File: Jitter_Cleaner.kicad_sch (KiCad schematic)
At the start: 38 parts, among them T1 TCM2-43X+, T3 TCM2-43X+, U18 SI5394, U20 TLV75733PDBV, U21 TLV75718PDBV, Y1 CX3225SB48000D0FPJC1

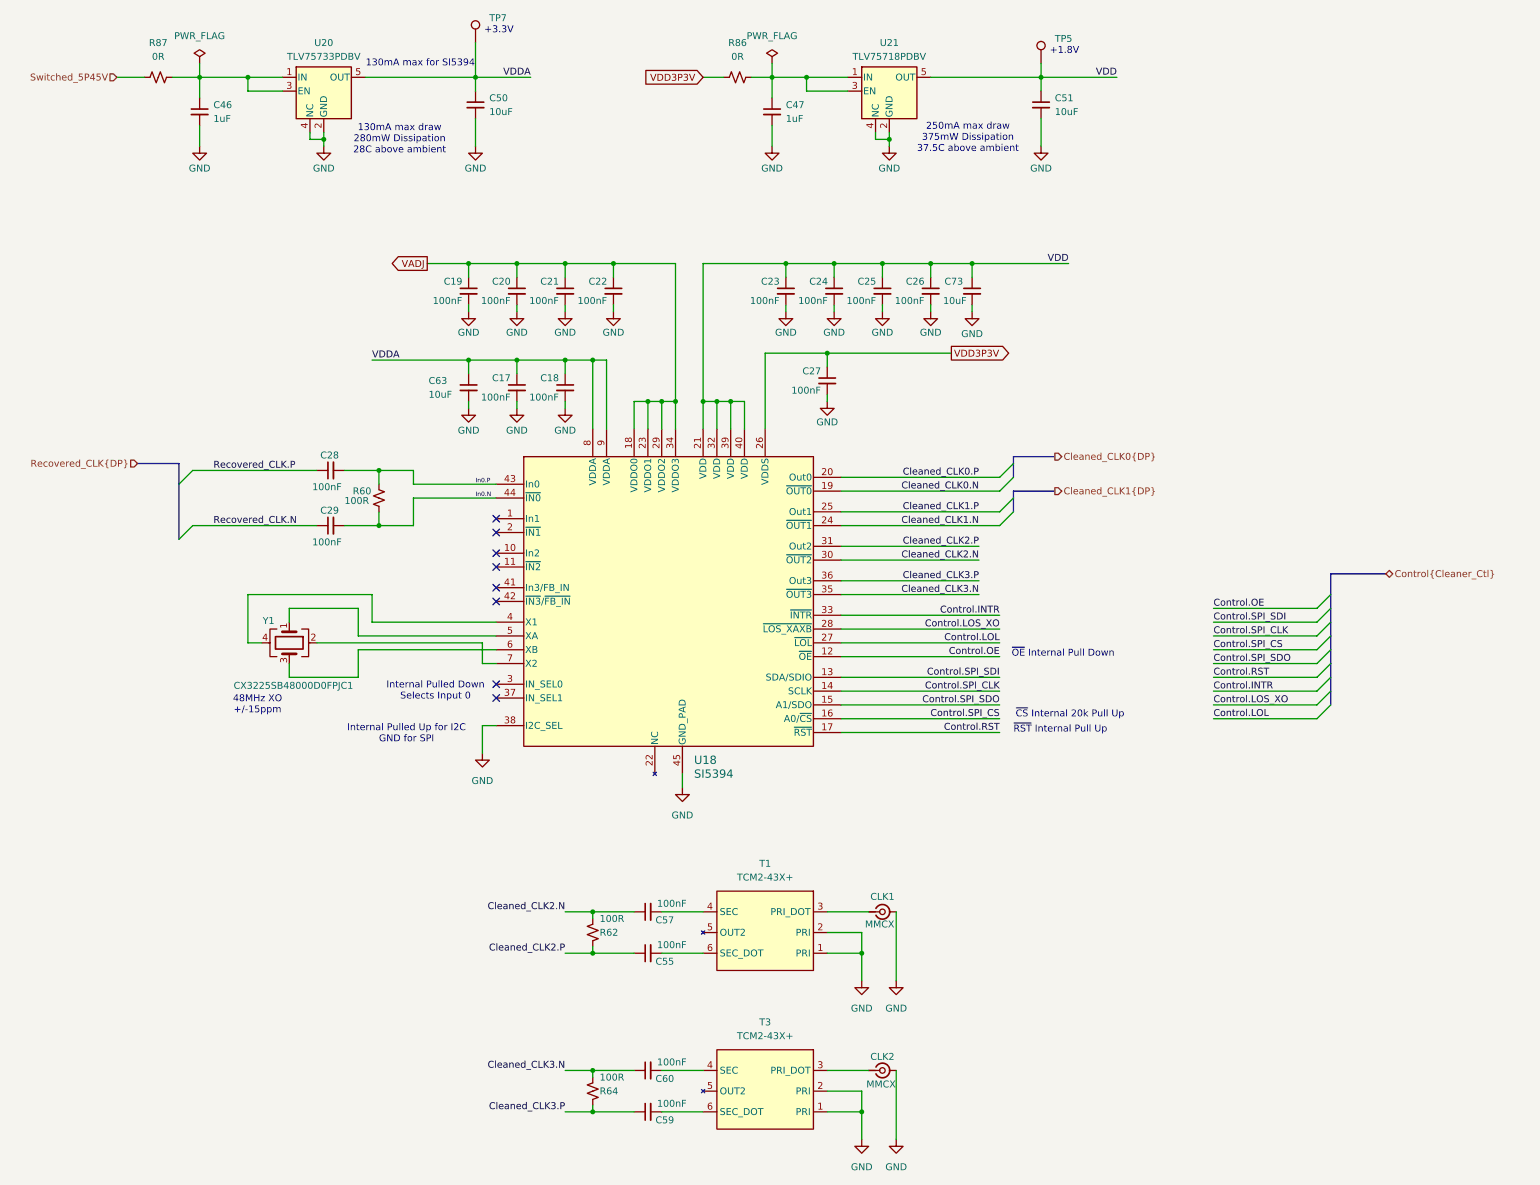
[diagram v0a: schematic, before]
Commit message: Updates after external review
- Changed Value of R66 & R67
- Added 100nF cap (C104) at input of U22
- Added GND via in center of U24 (like other LDO's)
- Changed 1nF Caps in Digital output section to 10nF
- Rounded pads of (T1-T4)
- Adjusted traces between T1-T4 and their respective MMCX connector
- Added FB1 & C136 at output of U22(5.45V switcher)
- Exchanged R88(0ohm) for a Ferrite Bead at input to U22(5.45V switcher)
- Revised layout of U22 area to more closely follow the data sheet.
- Exchanged R73&R42 at input to U44 for a ferrite bead (FB3)
- Exchanged R86/87/98/99 at input of TLV757 LDO for ferrite beads
- Added 1uF caps to VDD, VDDA, and VDDS power rails on Jitter Cleaner
- Changed C46,C47,C75,C77 from 1uF to 10uF caps
- Added Ferrite and 2 caps for each VDDO power rail on the jitter cleaners
- Adjusted layout around pint 26,27,28, of U18
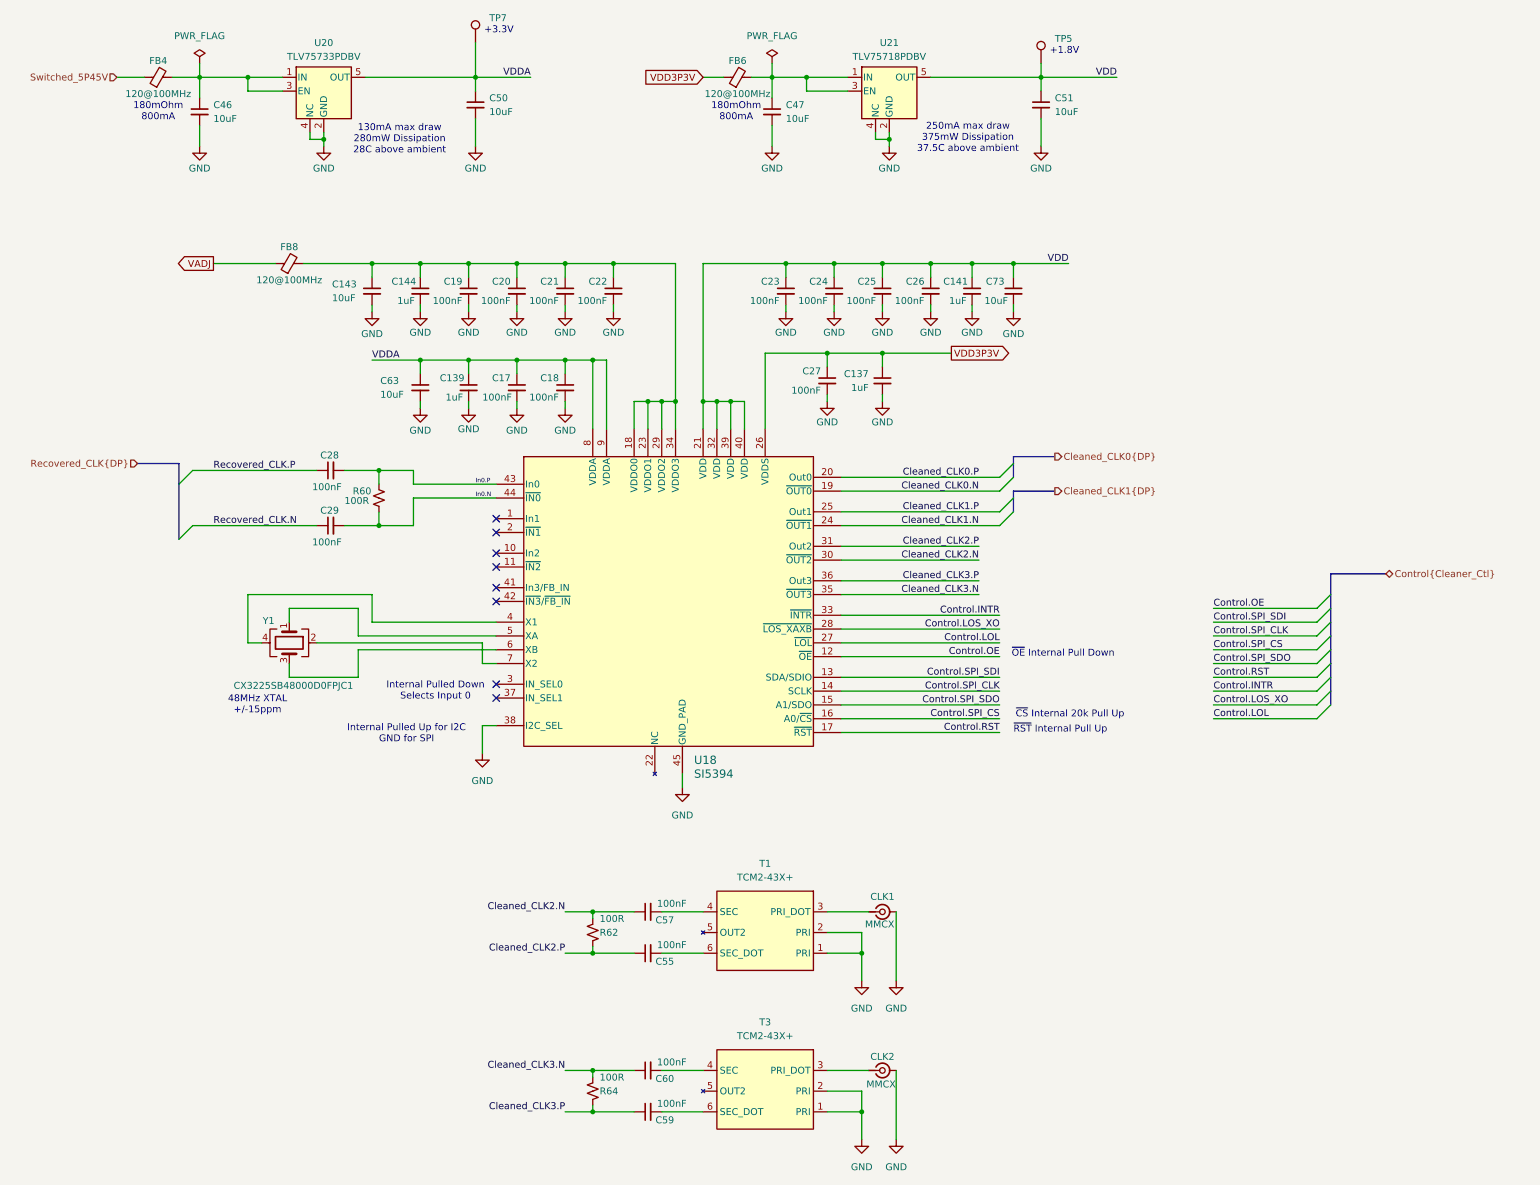
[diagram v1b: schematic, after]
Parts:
- removed R86, R87: 0R, Resistor_SMD:R_0603_1608Metric, symbol Device:R_Small_US
- added C137, C139, C141, C144: 1uF, Capacitor_SMD:C_0603_1608Metric, symbol Device:C_Small
- added C143: 10uF, Capacitor_SMD:C_0805_2012Metric, symbol Device:C_Small
- added FB4, FB6, FB8: 120@100MHz, Inductor_SMD:L_0603_1608Metric, symbol Device:FerriteBead_Small
- C46, C47: value 1uF -> 10uF; footprint Capacitor_SMD:C_0603_1608Metric -> Capacitor_SMD:C_0805_2012Metric; MPN GCM188R71C105KA64D -> GRM21BR61E106KA73L
- T1, T3: footprint RF_Mini-Circuits:Mini-Circuits_DB1627 -> rf-input-fmc:Mini-Circuits_DB1627_rounded_pads
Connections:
- net GND: now also C137.2, C139.2, C141.2, C143.2, C144.2
- net Switched_5P45V: now also FB4.1
- net VADJ: now also FB8.1; no longer C19.1, C20.1, C21.1, C22.1, U18.18 (VDDO0), U18.23 (VDDO1), U18.29 (VDDO2), U18.34 (VDDO3)
- net VDD: now also C141.1
- net VDD3P3V: now also C137.1, FB6.1
- net VDDA: now also C139.1
- net at C47.1, U21.1 (IN), U21.3 (EN): now also FB6.2
- net at C46.1, U20.1 (IN), U20.3 (EN): now also FB4.2
- new net: C143.1, C144.1, C19.1, C20.1, C21.1, C22.1, FB8.2, U18.18 (VDDO0), U18.23 (VDDO1), U18.29 (VDDO2), U18.34 (VDDO3)
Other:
- note added: "180mOhm 800mA"
- note added: "48MHz XTAL +/-15ppm"
- note removed: "130mA max for SI5394"
- note removed: "48MHz XO +/-15ppm"
- moved on the sheet: C63, C73

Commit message: Updates after external review
- Removed various construction lines on comments layer
- Corrected various 50ohm SE traces on external layers to 0.26mm width
- Shortened up longer traces where possible on external layers and LVDS (in5)
- Made routing of CLK signals to MMCX test ports consistant

- MAJOR UPDATE to XTAL (Y1&Y2)
This now follows the family reference manual to properly isolate the XTAL
This then required the following changes:
- Swapped layer In2 with In5 (to keep LVDS between GND layers)
- Swapped layer In3 with In4 (to keep LVDS between GND layers)
- Revised gate mapping of level shifted signals on the IC (no FMC pinout change)
- Significant revision to  routing around these area
- Rounded XTAL pads
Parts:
- Y1: footprint Crystal:Crystal_SMD_Abracon_ABM8AIG-4Pin_3.2x2.5mm -> rf-input-fmc:Crystal_SMD_Abracon_ABM8AIG-4Pin_3.2x2.5mm
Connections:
- net at U18.4 (X1), Y1.4: now also U18.7 (X2), Y1.2
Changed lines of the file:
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@@
 	(text "48MHz XTAL\n+/-15ppm"
 		(exclude_from_sim no)
-		(at 154.178 165.1 0)
+		(at 140.208 156.972 0)
 		(effects
 			(font
@@
 	)
 	(junction
+		(at 152.4 153.67)
+		(diameter 0)
+		(color 0 0 0 0)
+	)
+	(junction
 		(at 201.93 101.6)
 		(diameter 0)
@@
 	)
 	(junction
+		(at 167.64 144.78)
+		(diameter 0)
+		(color 0 0 0 0)
+	)
+	(junction
 		(at 236.22 109.22)
 		(diameter 0)
@@
 	(wire
 		(pts
-			(xy 165.1 153.67) (xy 195.58 153.67)
-		)
-		(stroke
-			(width 0)
-			(type default)
-		)
-	)
-	(wire
-		(pts
 			(xy 330.2 157.48) (xy 349.25 157.48)
 		)
@@
 	(wire
 		(pts
+			(xy 152.4 161.29) (xy 152.4 153.67)
+		)
+		(stroke
+			(width 0)
+			(type default)
+		)
+	)
+	(wire
+		(pts
 			(xy 238.76 109.22) (xy 236.22 109.22)
 		)
@@
 	(wire
 		(pts
+			(xy 173.99 157.48) (xy 173.99 161.29)
+		)
+		(stroke
+			(width 0)
+			(type default)
+		)
+	)
+	(wire
+		(pts
 			(xy 143.51 46.99) (xy 143.51 49.53)
 		)
@@
 	(wire
 		(pts
-			(xy 152.4 144.78) (xy 175.26 144.78)
+			(xy 152.4 144.78) (xy 167.64 144.78)
 		)
 		(stroke
@@
 	(wire
 		(pts
-			(xy 349.25 160.02) (xy 330.2 160.02)
+			(xy 173.99 161.29) (xy 152.4 161.29)
 		)
 		(stroke
@@
 		)
 	)
-	(bus
+	(wire
 		(pts
-			(xy 361.95 140.97) (xy 351.79 140.97)
+			(xy 349.25 160.02) (xy 330.2 160.02)
 		)
 		(stroke
@@
 		)
 	)
-	(wire
+	(bus
 		(pts
-			(xy 195.58 153.67) (xy 195.58 157.48)
+			(xy 361.95 140.97) (xy 351.79 140.97)
 		)
 		(stroke
@@
 	(wire
 		(pts
+			(xy 167.64 144.78) (xy 175.26 144.78)
+		)
+		(stroke
+			(width 0)
+			(type default)
+		)
+	)
+	(wire
+		(pts
 			(xy 255.27 49.53) (xy 262.89 49.53)
 		)
@@
 	(wire
 		(pts
+			(xy 167.64 153.67) (xy 167.64 144.78)
+		)
+		(stroke
+			(width 0)
+			(type default)
+		)
+	)
+	(wire
+		(pts
 			(xy 269.24 83.82) (xy 260.35 83.82)
 		)
@@
 	(wire
 		(pts
-			(xy 195.58 157.48) (xy 198.12 157.48)
+			(xy 173.99 157.48) (xy 198.12 157.48)
 		)
 		(stroke
@@
 	(wire
 		(pts
+			(xy 165.1 153.67) (xy 167.64 153.67)
+		)
+		(stroke
+			(width 0)
+			(type default)
+		)
+	)
+	(wire
+		(pts
 			(xy 259.08 100.33) (xy 259.08 102.87)
 		)
@@
 		)
 		(property "Value" "CX3225SB48000D0FPJC1"
-			(at 160.782 161.544 90)
+			(at 139.7 153.67 90)
 			(effects
 				(font
@@
 			)
 		)
-		(property "Footprint" "Crystal:Crystal_SMD_Abracon_ABM8AIG-4Pin_3.2x2.5mm"
+		(property "Footprint" "rf-input-fmc:Crystal_SMD_Abracon_ABM8AIG-4Pin_3.2x2.5mm"
 			(at 160.02 153.67 0)
 			(effects

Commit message: Small Tweaks
- Updated readme with kicad version
- fixed break in ground plane near Y2
- added exclusions with written exceptions for 4 DRC errors (where we grounded level shifter gates)
- Fixed whitespace at the end of MPNs
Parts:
- FB4, FB6, FB8: MPN BLM18AG121SN1D -> BLM18AG121SN1D
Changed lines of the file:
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@@
 			)
 		)
-		(property "MPN" "BLM18AG121SN1D "
+		(property "MPN" "BLM18AG121SN1D"
 			(at 135.89 49.53 90)
 			(effects
@@
 			)
 		)
-		(property "MPN" "BLM18AG121SN1D "
+		(property "MPN" "BLM18AG121SN1D"
 			(at 242.57 49.53 90)
 			(effects
@@
 			)
 		)
-		(property "MPN" "BLM18AG121SN1D "
+		(property "MPN" "BLM18AG121SN1D"
 			(at 160.02 83.82 90)
 			(effects

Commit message: Changed LDO gnd pours
-LDO ground pours had odd gerber outputs with thermal spokes.
These are now solid pours.

- Added small note on 100ohm termination
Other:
- note added: "Termination as descibed in Family Reference Manual page 21"
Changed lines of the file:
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@@
+		)
+	)
+	(text "Termination as descibed in  \nFamily Reference Manual page 21"
+		(exclude_from_sim no)
+		(at 168.656 138.176 0)
+		(effects
+			(font
+				(size 1.27 1.27)
+			)
 		)
 	)
